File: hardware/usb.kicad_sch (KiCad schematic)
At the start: 35 parts, among them J1 USB_A_Stacked, J2 USB_C_Receptacle_USB2.0_14P, J3 USB_C_Receptacle_USB2.0_14P, J4 USB_C_Receptacle_USB2.0_14P, U10 SY6280AAC, U11 SY6280AAC, U12 SY6280AAC, U13 TPD2EUSB30, U14 TPD2EUSB30, U15 TPD2EUSB30, U16 TPD2EUSB30, U17 HUSB237, U18 TPD2EUSB30, U9 SY6280AAC

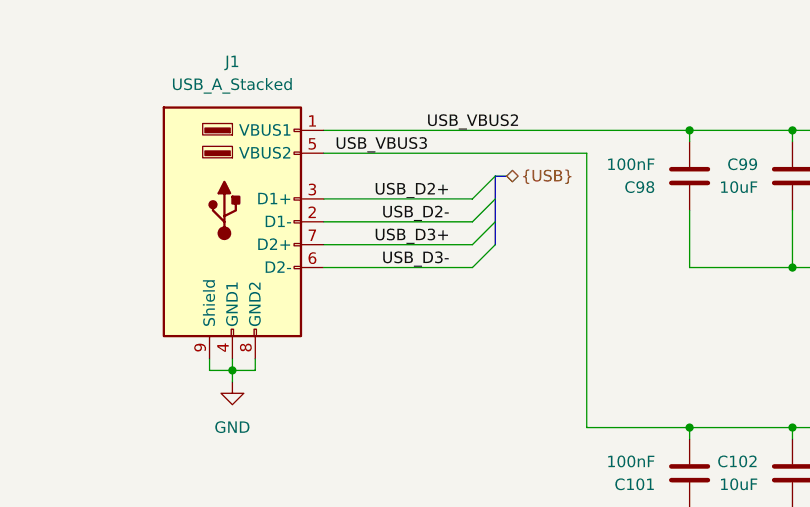
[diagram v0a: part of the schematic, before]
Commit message: Integrating DCDC converters
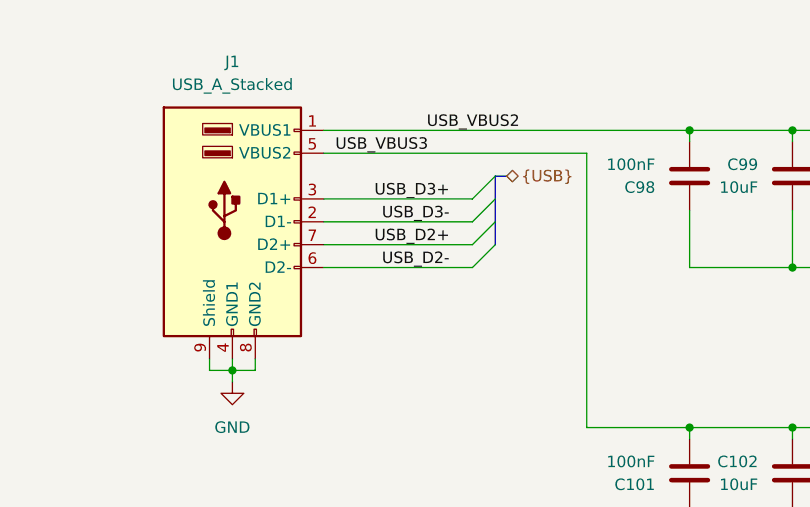
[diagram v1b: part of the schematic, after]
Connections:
- net USB_D2+: now also J1.7 (D2+); no longer J1.3 (D1+)
- net USB_D2-: now also J1.6 (D2-); no longer J1.2 (D1-)
- net USB_D3+: now also J1.3 (D1+); no longer J1.7 (D2+)
- net USB_D3-: now also J1.2 (D1-); no longer J1.6 (D2-)
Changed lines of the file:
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@@
 		)
 	)
-	(label "USB_D3-"
+	(label "USB_D2-"
 		(at 200.66 41.91 180)
 		(effects
@@
 		)
 	)
-	(label "USB_D2+"
+	(label "USB_D3+"
 		(at 200.66 34.29 180)
 		(effects
@@
 		)
 	)
-	(label "USB_D2-"
+	(label "USB_D3-"
 		(at 200.66 36.83 180)
 		(effects
@@
 		)
 	)
-	(label "USB_D3+"
+	(label "USB_D2+"
 		(at 200.66 39.37 180)
 		(effects

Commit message: Finished with V1!
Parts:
- J2, J3, J4: FT Position Offset 0,12.7 -> 0,-12.7
